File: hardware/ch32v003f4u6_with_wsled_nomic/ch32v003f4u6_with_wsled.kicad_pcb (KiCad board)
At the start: 2 copper layers, 35.6 x 44.5 mm, 23 parts, among them J2 PGM, J4 USB_C_Receptacle_USB2.0, J5 HOLE, J6 HOLE, U1 CH32V003F4U6, U2 3.3vReg

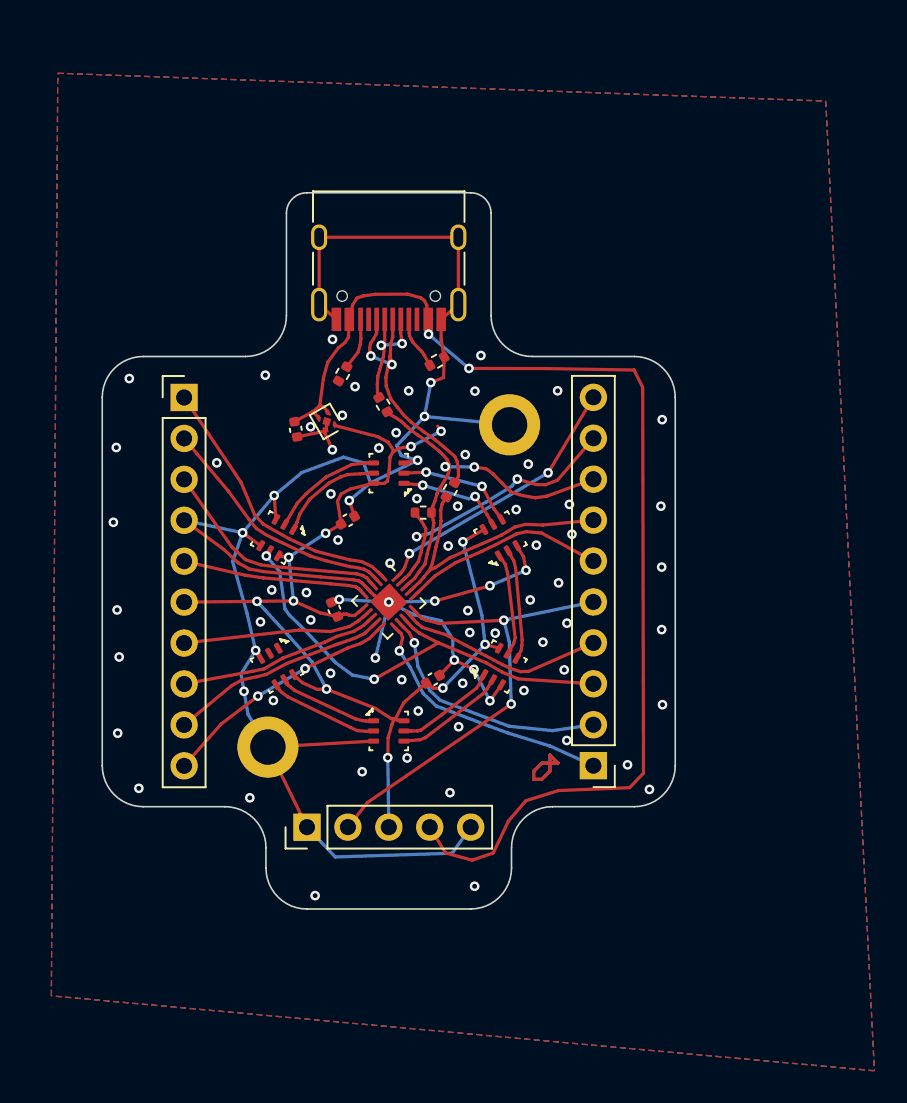
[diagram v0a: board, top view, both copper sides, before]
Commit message: Switch over to using a .c file instead of a .S file for the startup code.  Helps make order-of-compiling not matter.
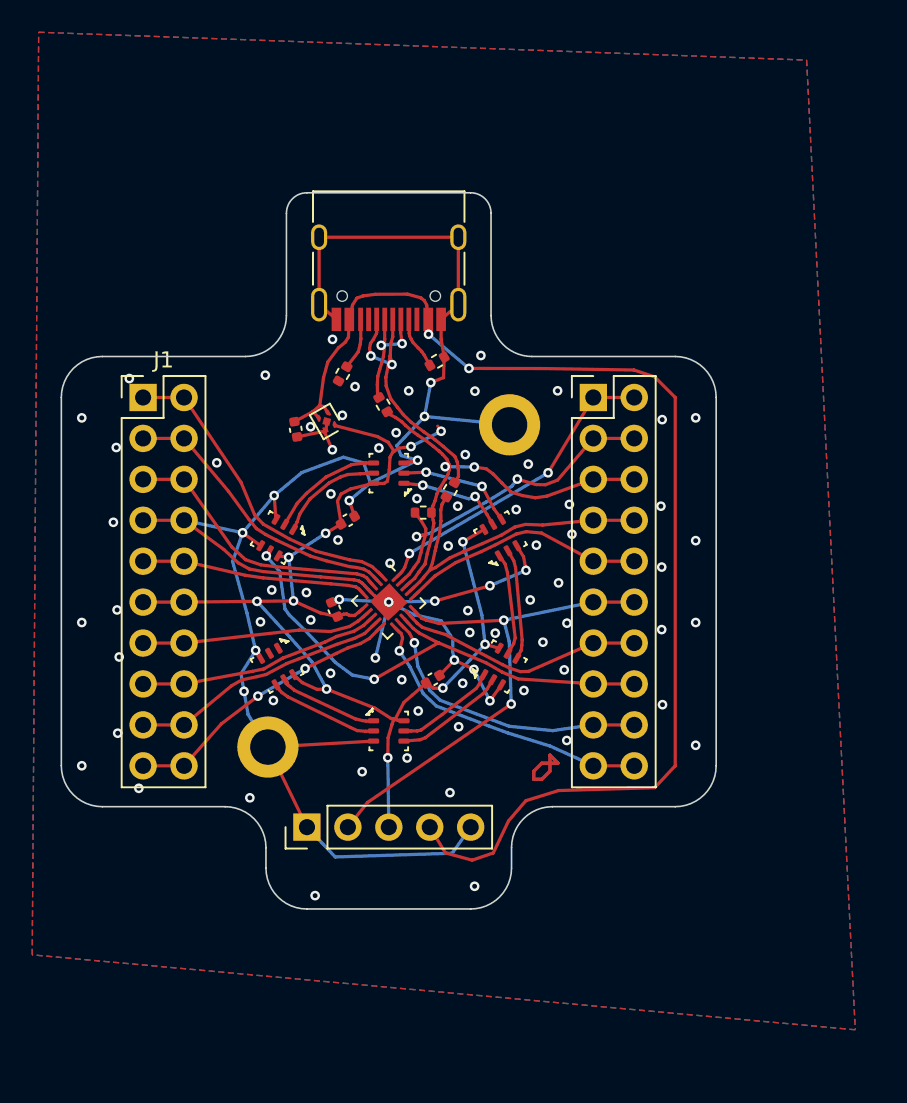
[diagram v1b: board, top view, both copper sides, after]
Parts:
- J1, J3: footprint Connector_PinHeader_2.54mm:PinHeader_1x10_P2.54mm_Vertical -> Connector_PinHeader_2.54mm:PinHeader_2x10_P2.54mm_Vertical
- moved J3 22.9 mm to (112.7, 87.3), turned to 0 degrees
- moved J1 2.55 mm to (84.8, 87.3)
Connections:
- J1 pad 10: PC3 -> PD0
- J1 pad 2: PA1 -> PD7NRST
- J1 pad 3: PA2 -> PA1
- J1 pad 4: GND -> PA1
- J1 pad 5: PD0 -> PA2
- J1 pad 6: VCC -> PA2
- J1 pad 7: PC0 -> GND
- J1 pad 8: PC1 -> GND
- J1 pad 9: PC2 -> PD0
- J3 pad 1: PC4 -> PD6
- J3 pad 10: PD6 -> PD2
- J3 pad 2: PC5 -> PD6
- J3 pad 3: PC6 -> DPU
- J3 pad 4: PC7 -> DPU
- J3 pad 5: SWIO -> D-
- J3 pad 6: PD2 -> D-
- J3 pad 8: D- -> D+
- J3 pad 9: DPU -> PD2
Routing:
- net +5V: track 72.1 -> 75.1 mm
- net PD7NRST: track 17.5 -> 20.0 mm
- net PC3: track 15.1 -> 17.6 mm
- net VCC: track 71.9 -> 74.4 mm
- net PD6: track 17.1 -> 19.6 mm
- net PD2: track 12.7 -> 15.2 mm
- net PD0: track 11.4 -> 14.0 mm
- net PC7: track 12.7 -> 15.3 mm
- net PC6: track 28.5 -> 31.1 mm
- net PC5: track 15.4 -> 17.9 mm
- net PC4: track 16.2 -> 18.8 mm
- net PC2: track 13.7 -> 16.2 mm
- net PC1: track 12.5 -> 15.0 mm
- net PC0: track 11.7 -> 14.3 mm
- net DPU: track 18.8 -> 21.3 mm
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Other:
- board size 35.6 x 44.5 mm -> 40.6 x 44.5 mm
